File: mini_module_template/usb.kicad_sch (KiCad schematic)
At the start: 16 parts, among them J1 USB_C_Receptacle_USB2.0, Q2 S9013, U3 USBLC6-2SC6, U7 SL2.1A

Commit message: Leyout rev 1
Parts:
- removed Q2: S9013, Package_TO_SOT_SMD:SOT-23, symbol Device:Q_NPN_BEC
- removed R39: 1K5, Resistor_SMD:R_0402_1005Metric, symbol Device:R
- added D1: D_Schottky, Diode_SMD:D_SMA, symbol Device:D_Schottky
- added R43: 22R, Resistor_SMD:R_0402_1005Metric, symbol Device:R
- C34: renamed from C24; footprint Capacitor_SMD:C_0603_1608Metric -> Capacitor_SMD:C_0402_1005Metric
- C35: renamed from C25; footprint Capacitor_SMD:C_0603_1608Metric -> Capacitor_SMD:C_0402_1005Metric
- R40: value 10k -> 22R; LCSC C25744 -> (none)
- R41: value 39k -> 22R; LCSC C25783 -> (none)
- R42: value 100R -> 22R; LCSC C25076 -> (none)
- U6: renamed from U3; value USBLC6-2SC6 -> IP4220CZ6
- U7: footprint local_footpritn:SO16 -> Package_SO:SOP-16_3.9x9.9mm_P1.27mm
- renumbered C13 to C33, J1 to J4, R5 to R31, R6 to R32, R7 to R33, R8 to R34, R4 to R35
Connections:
- net USB_RENUM is gone; now on net USB_MCU_D-: R42.1
- net +5V: now also D1.1 (K); no longer R40.2
- net GND: no longer R41.1
- net USB_MCU_D+: now also R43.1; no longer U7.8 (DP1)
- net USB_MCU_D-: no longer U7.7 (DM1)
- net USB_STLINK_D+: now also R41.1; no longer U7.6 (DP2)
- net USB_STLINK_D-: now also R40.2; no longer U7.5 (DM2)
- net V_BUS: no longer J4.A4 (VBUS), J4.A9 (VBUS), J4.B4 (VBUS), J4.B9 (VBUS)
- new net: D1.2 (A), J4.A4 (VBUS), J4.A9 (VBUS), J4.B4 (VBUS), J4.B9 (VBUS)
- new net: R42.2, U7.7 (DM1)
- new net: R40.1, U7.5 (DM2)
- new net: R43.2, U7.8 (DP1)
- new net: R41.2, U7.6 (DP2)
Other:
- note removed: "FORCE RENUMERATION OF USB DEVICES"

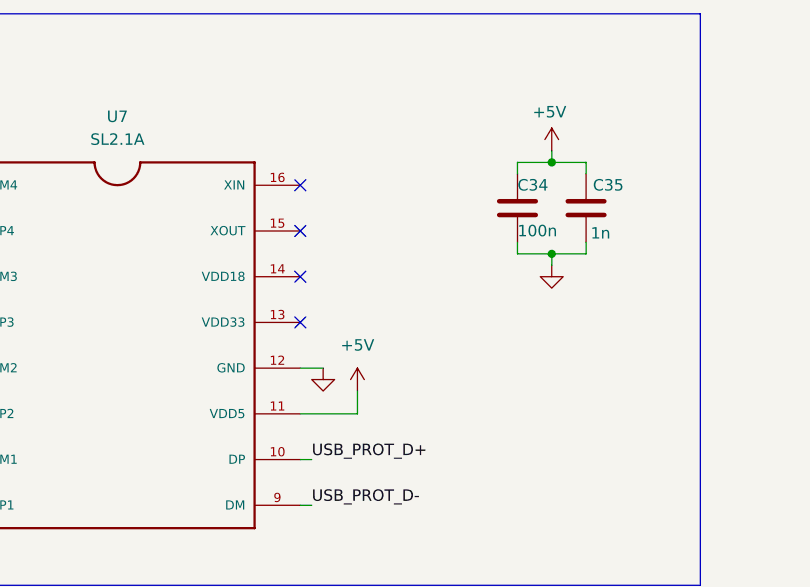
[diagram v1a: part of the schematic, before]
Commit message: addded crystal to usb hub. added connection tabs to stm+stlink
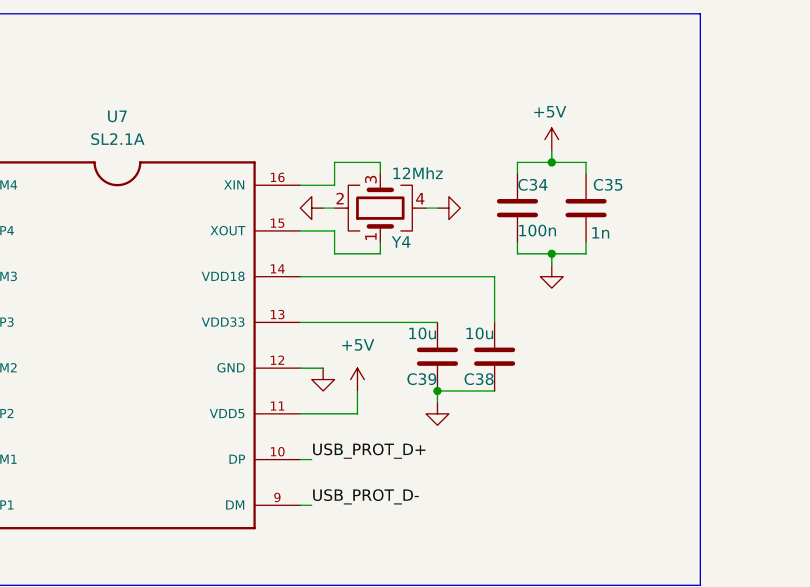
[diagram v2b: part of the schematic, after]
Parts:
- added C38, C39: 10u, Capacitor_SMD:C_0805_2012Metric, symbol Device:C
- added Y4: 12Mhz, Crystal:Crystal_SMD_3225-4Pin_3.2x2.5mm, symbol Device:Crystal_GND24
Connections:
- net GND: now also C38.1, C39.1, Y4.2, Y4.4
- net at U7.13 (VDD33): now also C39.2
- net at U7.14 (VDD18): now also C38.2
- net at U7.15 (XOUT): now also Y4.1
- net at U7.16 (XIN): now also Y4.3
- no-connect marks 10 -> 6

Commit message: a
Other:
- note added: "CL=15pF Cs=5pF C=2*(CL-Cs)=20"
- moved on the sheet: C34, C35, Y4

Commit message: rev 1.0 finished
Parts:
- added C40: 100n, Capacitor_SMD:C_0402_1005Metric, symbol Device:C
- added C41: 1n, Capacitor_SMD:C_0402_1005Metric, symbol Device:C
- added R45: 10k, Resistor_SMD:R_0402_1005Metric, symbol Device:R
- added R46, R47: 22R, Resistor_SMD:R_0402_1005Metric, symbol Device:R
- added U8: TS3USB30EDGSR, Package_SO:VSSOP-10_3x3mm_P0.5mm, symbol Interface_USB:TS3USB30EDGSR
- C33: footprint Capacitor_SMD:C_0805_2012Metric -> Capacitor_SMD:C_0402_1005Metric
- C38, C39: footprint Capacitor_SMD:C_0805_2012Metric -> Capacitor_SMD:C_0603_1608Metric
- R35: footprint Resistor_SMD:R_0603_1608Metric -> Resistor_SMD:R_0402_1005Metric
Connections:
- net V_BUS is gone; now on net VBUS: U6.5 (VBUS)
- net GND: now also C40.2, C41.2, R45.1, U8.5 (GND)
- net USB_CONN_D+: now also R34.1, U6.3 (I/O2)
- net USB_CONN_D-: now also R33.1, U6.1 (I/O1)
- net USB_PROT_D+: now also U8.3 (D2+); no longer U7.10 (DP)
- net USB_PROT_D-: now also U8.7 (D2-); no longer U7.9 (DM)
- net VBUS: now reaches D1.2 (A), J4.A4 (VBUS), J4.A9 (VBUS), J4.B4 (VBUS), J4.B9 (VBUS)
- net VBUS: now also U8.1 (S)
- net at U7.7 (DM1): now also R46.1; no longer R42.2
- net at U7.5 (DM2): now also R42.2; no longer R40.1
- net at R43.2: now also U7.6 (DP2); no longer U7.8 (DP1)
- net at U7.3 (DM3): now also R40.1
- net at U7.4 (DP3): now also R41.2
- new net: R45.2, U8.9 (~{OE})
- new net: R47.2, U7.8 (DP1)
- new net +3V3: C40.1, C41.1, U8.10 (VCC)
- new net USB_DOWNSTREM_D+: R47.1
- new net USB_DOWNSTREM_D-: R46.2
- new net USB_SWITCH_D+: U8.2 (D1+)
- new net USB_SWITCH_D-: U8.8 (D1-)
- new net USB_UPSTREAM_D+: U7.10 (DP), U8.4 (D+)
- new net USB_UPSTREAM_D-: U7.9 (DM), U8.6 (D-)
- no-connect marks 6 -> 4
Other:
- note added: "USB SWITCH"
- moved on the sheet: R33, R34, U6

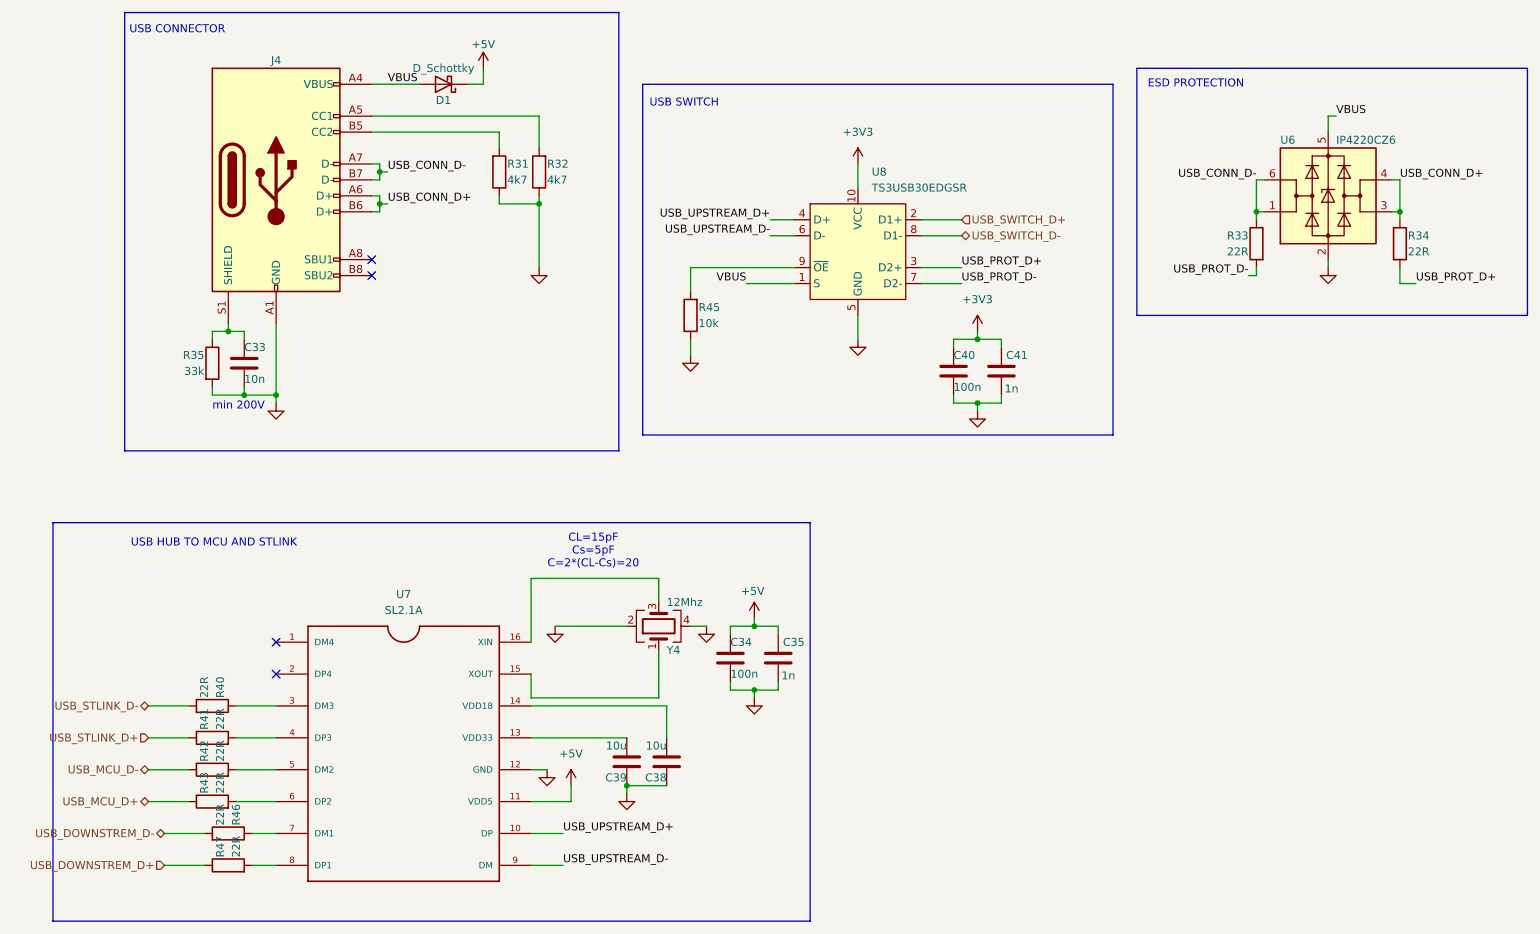
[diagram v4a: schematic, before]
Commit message: revison C, aded 2 can support and gight voltage input stepdown
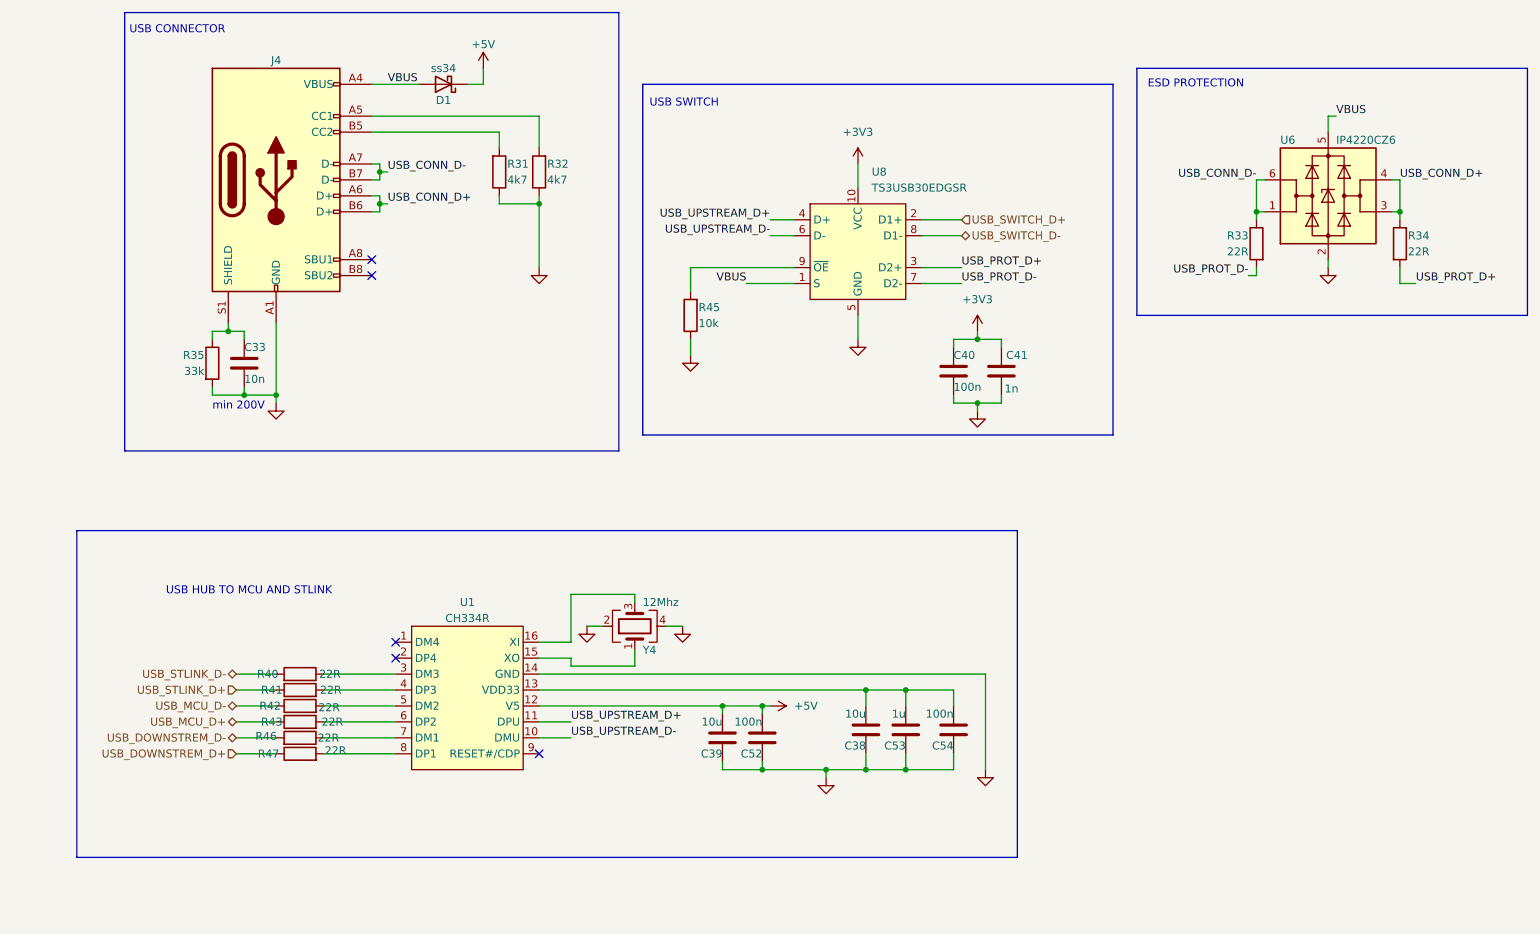
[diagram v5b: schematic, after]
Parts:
- removed C34: 100n, Capacitor_SMD:C_0402_1005Metric, symbol Device:C
- removed C35: 1n, Capacitor_SMD:C_0402_1005Metric, symbol Device:C
- removed U7: SL2.1A, Package_SO:SOP-16_3.9x9.9mm_P1.27mm, symbol SL2.1A:SL2.1A
- added C52: 100n, Capacitor_SMD:C_0603_1608Metric, symbol Device:C
- added C53: 1u, Capacitor_SMD:C_0603_1608Metric, symbol Device:C
- added C54: 100n, Capacitor_SMD:C_0402_1005Metric, symbol Device:C
- added U1: CH334R, Package_SO:QSOP-16_3.9x4.9mm_P0.635mm, symbol WCH_USB:CH334R
- D1: value D_Schottky -> ss34
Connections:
- net +5V: now also C39.2, C52.2, U1.12 (V5)
- net GND: now also C52.1, C53.1, C54.1, U1.14 (GND)
- net USB_UPSTREAM_D+: now also U1.11 (DPU)
- net USB_UPSTREAM_D-: now also U1.10 (DMU)
- net at R46.1: now also U1.7 (DM1)
- net at R42.2: now also U1.5 (DM2)
- net at R41.2: now also U1.4 (DP3)
- net at R43.2: now also U1.6 (DP2)
- net at Y4.1: now also U1.15 (XO)
- net at Y4.3: now also U1.16 (XI)
- net at R47.2: now also U1.8 (DP1)
- net at C38.2: now also C53.2, C54.2, U1.13 (VDD33)
- net at R40.1: now also U1.3 (DM3)
- no-connect marks 4 -> 5
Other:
- note removed: "CL=15pF Cs=5pF C=2*(CL-Cs)=20"
- moved on the sheet: C38, C39, R40, R41, R42, R43, R46, R47, Y4

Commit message: updaet schematic
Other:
- company: (none) -> Patryk Dudziński
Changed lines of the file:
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@@
 	(title_block
 		(title "USB")
+		(date "2025-01-10")
+		(rev "1.0")
+		(company "Patryk Dudziński")
 	)
 	(junction
@@
 	(label "USB_CONN_D+"
 		(at 231.14 48.26 0)
-		(fields_autoplaced yes)
 		(effects
 			(font
@@
 	(label "VBUS"
 		(at 127 64.77 180)
-		(fields_autoplaced yes)
 		(effects
 			(font
@@
 	(label "USB_UPSTREAM_D-"
 		(at 99.06 137.16 0)
-		(fields_autoplaced yes)
 		(effects
 			(font
@@
 	(label "USB_UPSTREAM_D+"
 		(at 130.81 54.61 180)
-		(fields_autoplaced yes)
 		(effects
 			(font
@@
 	(label "USB_CONN_D+"
 		(at 69.85 52.07 0)
-		(fields_autoplaced yes)
 		(effects
 			(font
@@
 	(label "USB_PROT_D-"
 		(at 207.01 63.5 180)
-		(fields_autoplaced yes)
 		(effects
 			(font
@@
 	(label "VBUS"
 		(at 220.98 38.1 0)
-		(fields_autoplaced yes)
 		(effects
 			(font
@@
 	(label "USB_PROT_D+"
 		(at 161.29 62.23 0)
-		(fields_autoplaced yes)
 		(effects
 			(font
@@
 	(label "USB_CONN_D-"
 		(at 69.85 46.99 0)
-		(fields_autoplaced yes)
 		(effects
 			(font
@@
 	(label "USB_PROT_D-"
 		(at 161.29 64.77 0)
-		(fields_autoplaced yes)
 		(effects
 			(font
@@
 	(label "VBUS"
 		(at 69.85 33.02 0)
-		(fields_autoplaced yes)
 		(effects
 			(font
@@
 	(label "USB_CONN_D-"
 		(at 208.28 48.26 180)
-		(fields_autoplaced yes)
 		(effects
 			(font
@@
 	(label "USB_PROT_D+"
 		(at 233.68 64.77 0)
-		(fields_autoplaced yes)
 		(effects
 			(font
@@
 	(label "USB_UPSTREAM_D+"
 		(at 99.06 134.62 0)
-		(fields_autoplaced yes)
 		(effects
 			(font
@@
 	(label "USB_UPSTREAM_D-"
 		(at 130.81 57.15 180)
-		(fields_autoplaced yes)
 		(effects
 			(font
@@
 		(shape bidirectional)
 		(at 45.72 132.08 180)
-		(fields_autoplaced yes)
 		(effects
 			(font
@@
 		(shape bidirectional)
 		(at 45.72 137.16 180)
-		(fields_autoplaced yes)
 		(effects
 			(font
@@
 		(shape input)
 		(at 45.72 129.54 180)
-		(fields_autoplaced yes)
 		(effects
 			(font
@@
 		(shape bidirectional)
 		(at 45.72 127 180)
-		(fields_autoplaced yes)
 		(effects
 			(font
@@
 		(shape input)
 		(at 45.72 139.7 180)
-		(fields_autoplaced yes)
 		(effects
 			(font
@@
 		(shape input)
 		(at 161.29 54.61 0)
-		(fields_autoplaced yes)
 		(effects
 			(font
@@
 		(shape bidirectional)
 		(at 161.29 57.15 0)
-		(fields_autoplaced yes)
 		(effects
 			(font
@@
 		(shape bidirectional)
 		(at 45.72 134.62 180)
-		(fields_autoplaced yes)
-		(effects
-			(font
+		(effects
+			(font
